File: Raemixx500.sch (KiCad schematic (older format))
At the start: 3 parts

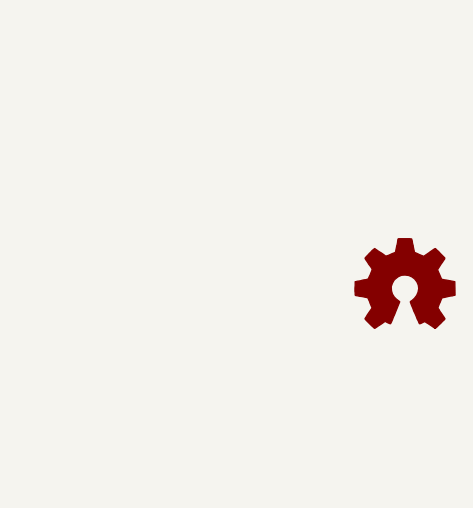
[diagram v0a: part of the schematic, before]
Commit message: Replace OSHW logo with CC-BY-NC-SA logo - Ready for V2B Sigh.
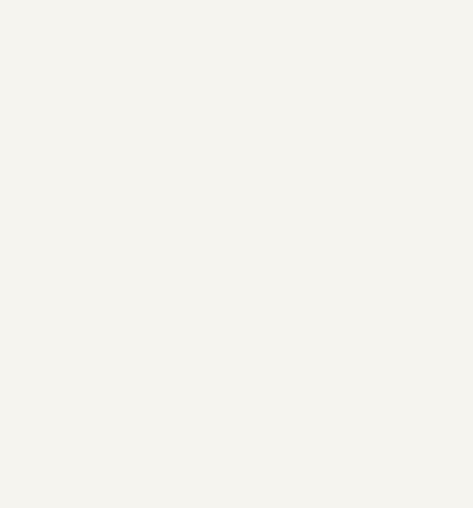
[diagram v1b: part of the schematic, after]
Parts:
- V0: footprint Symbol:OSHW-Logo2_14.6x12mm_SilkScreen -> Raemixx500:cc_by_nc_sa
- V1: footprint Symbol:KiCad-Logo2_8mm_SilkScreen -> Symbol:KiCad-Logo2_6mm_SilkScreen
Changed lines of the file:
@@
 Sheet 1 14
 Title "Rämixx500"
-Date "2020-04-11"
+Date "2021-05-26"
 Rev "1"
 Comp "SukkoPera"
@@
 $EndSheet
 $Comp
-L Graphic:Logo_Open_Hardware_Small #LOGO1
-U 1 1 5ED3E3EE
-P 10865 6860
-F 0 "#LOGO1" H 10865 7135 50  0001 C CNN
-F 1 "Logo_Open_Hardware_Small" H 10865 6635 50  0001 C CNN
-F 2 "" H 10865 6860 50  0001 C CNN
-F 3 "~" H 10865 6860 50  0001 C CNN
-	1    10865 6860
-	1    0    0    -1
-$EndComp
-$Comp
 L void:Void V0
 U 1 1 5ED3E7FB
@@
 F 0 "V0" H 6458 7686 50  0000 L CNN
 F 1 "OSHW_LOGO" H 6458 7595 50  0000 L CNN
-F 2 "Symbol:OSHW-Logo2_14.6x12mm_SilkScreen" H 6380 7640 50  0001 C CNN
+F 2 "Raemixx500:cc_by_nc_sa" H 6380 7640 50  0001 C CNN
 F 3 "" H 6380 7640 50  0001 C CNN
 F 4 "SKIP" H 6380 7640 50  0001 C CNN "MFG Name"
@@
 F 0 "V1" H 6458 7476 50  0000 L CNN
 F 1 "KICAD_LOGO" H 6458 7385 50  0000 L CNN
-F 2 "Symbol:KiCad-Logo2_8mm_SilkScreen" H 6380 7430 50  0001 C CNN
+F 2 "Symbol:KiCad-Logo2_6mm_SilkScreen" H 6380 7430 50  0001 C CNN
 F 3 "" H 6380 7430 50  0001 C CNN
 F 4 "SKIP" H 6380 7430 50  0001 C CNN "MFG Name"
